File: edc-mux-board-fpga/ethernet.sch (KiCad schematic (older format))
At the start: 38 parts, among them U62 W5500

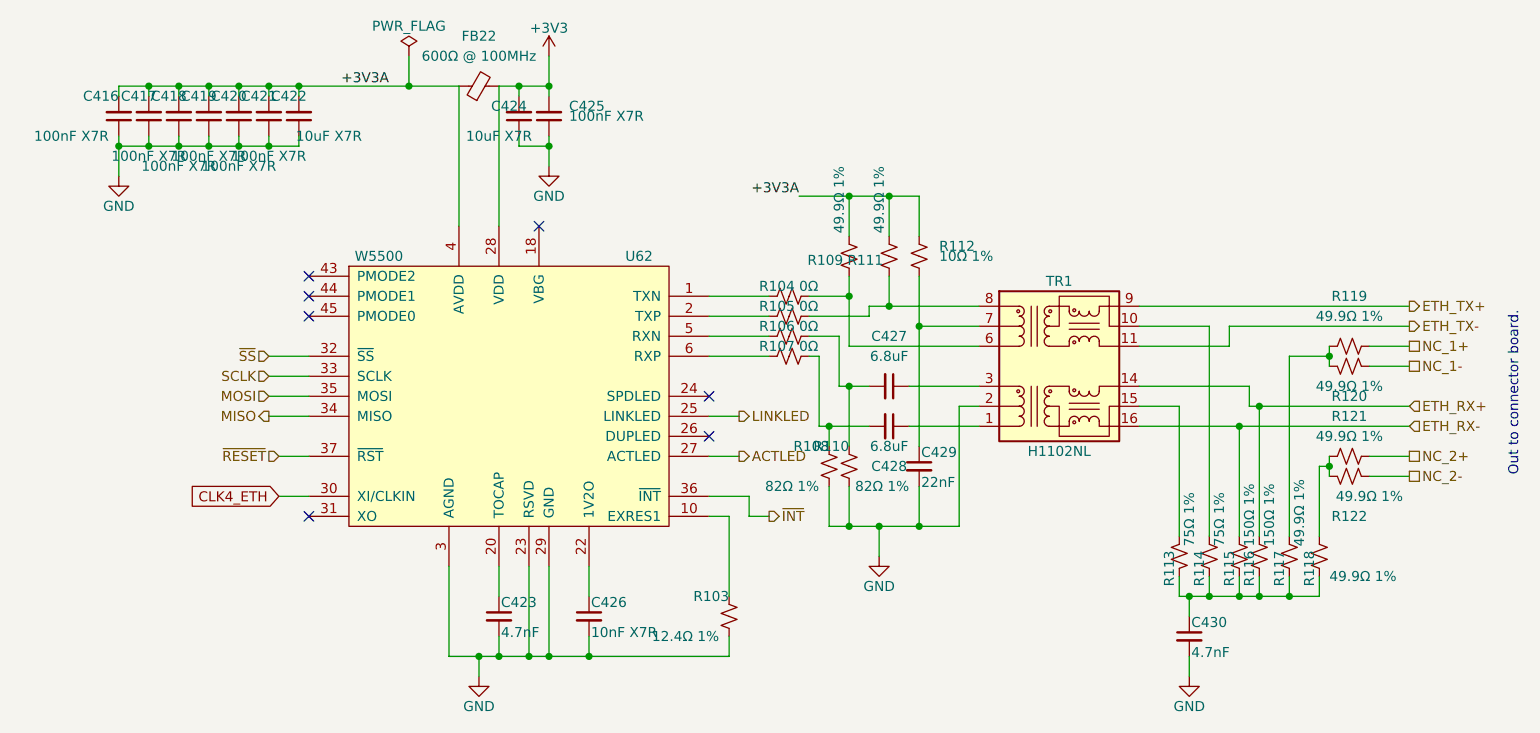
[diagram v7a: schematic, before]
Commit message: Reannotating and adding more fields to components
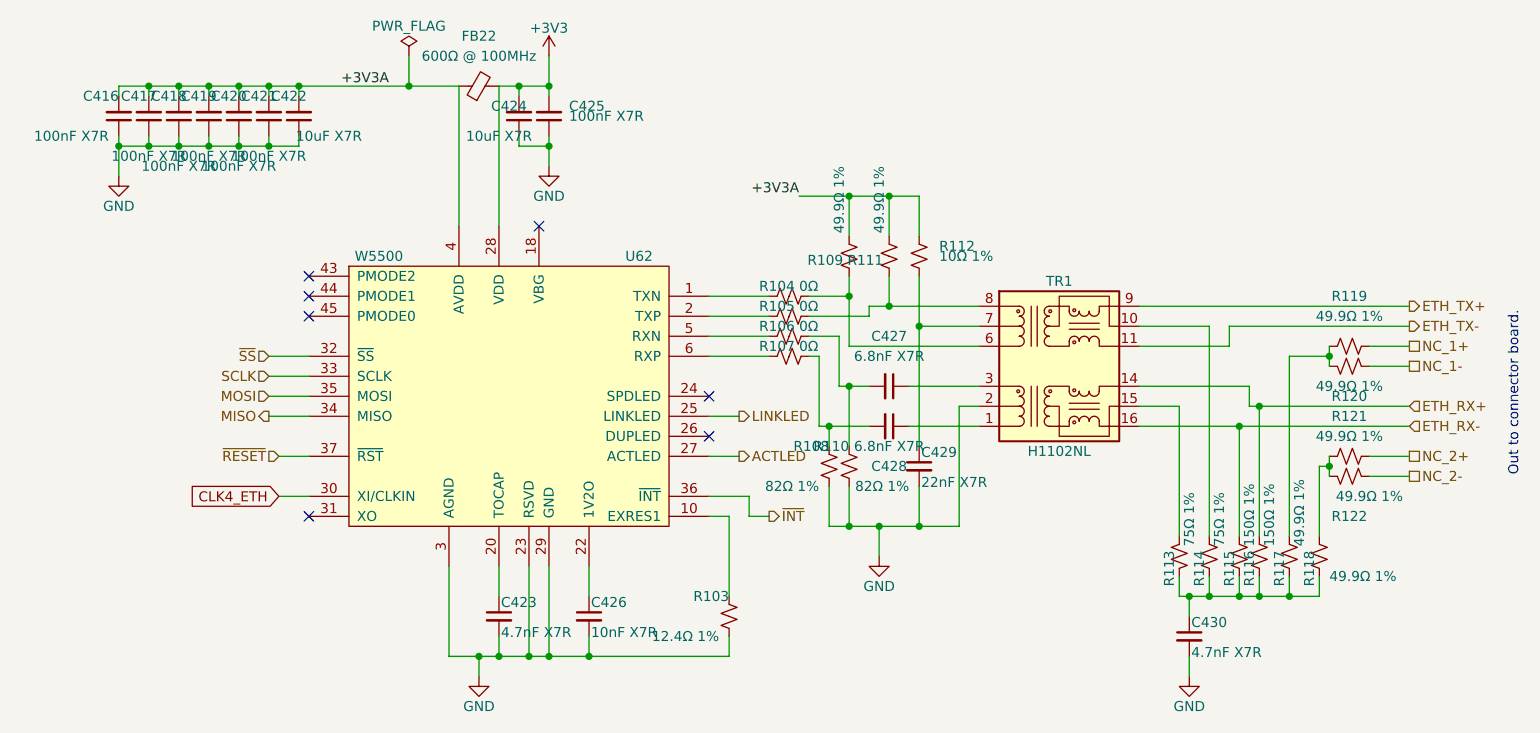
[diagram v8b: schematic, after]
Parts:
- C416, C417, C418, C419, C420, C421, C425: Characteristics (none) -> CAP CER 0.1UF 25V X7R 0603; Description (none) -> MLCC Capacitor; Manufacturer (none) -> Kemet; Manufacturers Part Number (none) -> C0603C104J3RACAUTO
- C422, C424: Characteristics (none) -> CAP CER 10UF 25V X7R 1206; Description (none) -> MLCC Capacitor
- C423, C430: value 4.7nF -> 4.7nF X7R; footprint Capacitor_SMD:C_0603_1608Metric -> Capacitor_SMD:C_0402_1005Metric; Characteristics (none) -> CAP CER 0402 4.7NF 25V X7R 5%; Description (none) -> MLCC Capacitor; Manufacturer (none) -> Kemet; Manufacturers Part Number (none) -> C0402C472J3RECAUTO; Package ID 0603in/1608mm -> 0402in/1005mm
- C426: Characteristics (none) -> CAP CER 10000PF 25V X7R 0402; Description (none) -> MLCC Capacitor; Manufacturer (none) -> Kemet; Manufacturers Part Number (none) -> C0402C103J3RACAUTO
- C427, C428: value 6.8uF -> 6.8nF X7R; footprint Capacitor_SMD:C_0805_2012Metric -> Capacitor_SMD:C_0402_1005Metric; Characteristics (none) -> 6800pF ±5% 25V Ceramic Capacitor X7R 0402 (1005 Metric); Description (none) -> MLCC Capacitor; Manufacturer (none) -> AVX; Manufacturers Part Number (none) -> 04023C682JAT2A; Package ID 0805in/2012mm -> 0402in/1005mm
- C429: value 22nF -> 22nF X7R; footprint Capacitor_SMD:C_0603_1608Metric -> Capacitor_SMD:C_0402_1005Metric; Characteristics (none) -> CAP CER 0402 22NF 25V X7R 5%; Description (none) -> MLCC Capacitor; Manufacturer (none) -> Kemet; Manufacturers Part Number (none) -> C0402C223J3RECAUTO7411; Package ID 0603in/1608mm -> 0402in/1005mm
- FB22: footprint Capacitor_SMD:C_0805_2012Metric -> Inductor_SMD:L_0805_2012Metric; Characteristics (none) -> 600 Ohms @ 100MHz 1 Signal Line Ferrite Bead 0805 (2012 Met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; Description (none) -> Ferrite Bead; Manufacturers Part Number BLM21AG601BH1 -> BLM21AG601SZ1D
- R103, R104, R105, R106, R107, R108, R109, R110, R111, R112, R113, R114, R115, R116, R117, R118, R119, R120, R121, R122: Description (none) -> Resistor
- TR1: Description (none) -> Ethernet Transformer; Package ID (none) -> H1102NL
- U62: Description (none) -> SPI Ethernet MAC/PHY; Manufacturer (none) -> Wiznet; Manufacturers Part Number (none) -> W5500; Package ID (none) -> TQFP48
